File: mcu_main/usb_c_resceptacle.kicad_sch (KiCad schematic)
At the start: 8 parts, among them U2 USB_C_connector

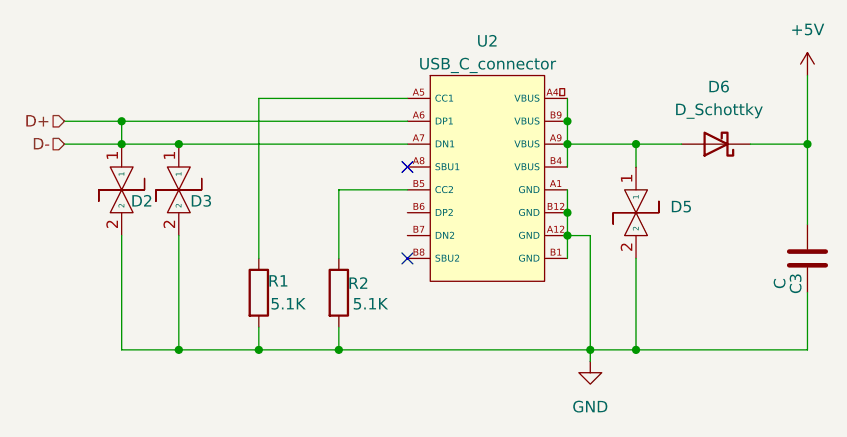
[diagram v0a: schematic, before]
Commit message: adding boot-reset buttons and microsd card spi
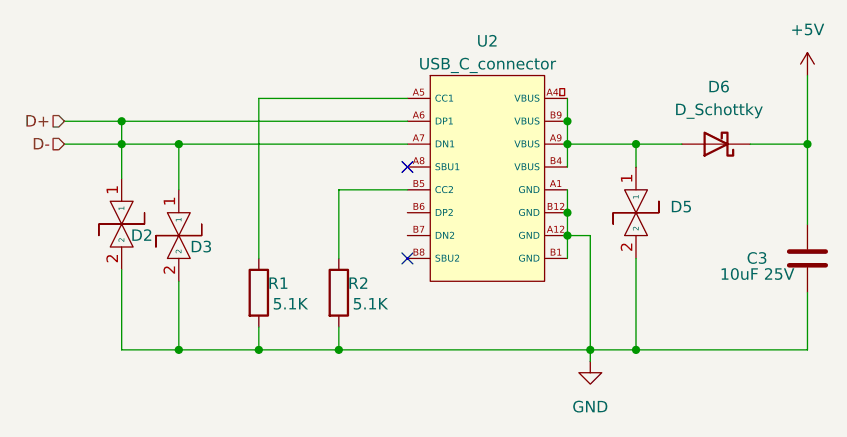
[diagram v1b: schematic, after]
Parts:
- C3: value C -> 10uF 25V
- D2, D3, D5: footprint (none) -> Diode_SMD:D_SOD-882
- R1, R2: footprint (none) -> Resistor_SMD:R_0805_2012Metric_Pad1.20x1.40mm_HandSolder
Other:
- moved on the sheet: D2, D3
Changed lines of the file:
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@@
+	(wire
+		(pts
+			(xy 121.92 96.52) (xy 121.92 91.44)
+		)
+		(stroke
+			(width 0)
+			(type default)
+		)
+	)
 	(wire
 		(pts
@@
 	(wire
 		(pts
+			(xy 115.57 95.25) (xy 115.57 91.44)
+		)
+		(stroke
+			(width 0)
+			(type default)
+		)
+	)
+	(wire
+		(pts
 			(xy 147.32 96.52) (xy 139.7 96.52)
 		)
@@
 	(wire
 		(pts
-			(xy 115.57 101.6) (xy 115.57 114.3)
+			(xy 115.57 105.41) (xy 115.57 114.3)
 		)
 		(stroke
@@
 	(wire
 		(pts
-			(xy 121.92 101.6) (xy 121.92 114.3)
+			(xy 121.92 106.68) (xy 121.92 114.3)
 		)
 		(stroke
@@
 	(symbol
 		(lib_id "Custom_symbols:ESD_protection_TVS_RCLAMP0521P-N")
-		(at 115.57 96.52 270)
+		(at 115.57 100.33 270)
 		(unit 1)
 		(exclude_from_sim no)
@@
 		(dnp no)
 		(property "Reference" "D2"
-			(at 116.586 97.79 90)
+			(at 116.586 101.6 90)
 			(effects
 				(font
@@
 		)
 		(property "Value" "~"
-			(at 119.38 97.79 90)
+			(at 119.38 101.6 90)
 			(effects
 				(font
@@
 			)
 		)
-		(property "Footprint" ""
-			(at 115.57 96.52 0)
-			(effects
-				(font
-					(size 1.27 1.27)
-				)
-				(hide yes)
-			)
-		)
-		(property "Datasheet" ""
-			(at 115.57 96.52 0)
+		(property "Footprint" "Diode_SMD:D_SOD-882"
+			(at 115.57 100.33 0)
+			(effects
+				(font
+					(size 1.27 1.27)
+				)
+				(hide yes)
+			)
+		)
+		(property "Datasheet" "https://www.lcsc.com/datasheet/lcsc_datasheet_2304171630_BORN-RCLAMP0521P-N_C316043.pdf"
+			(at 115.57 100.33 0)
 			(effects
 				(font
@@
 		)
 		(property "Description" ""
-			(at 115.57 96.52 0)
+			(at 115.57 100.33 0)
 			(effects
 				(font
@@
 			)
 		)
-		(property "Footprint" ""
+		(property "Footprint" "Diode_SMD:D_SOD-882"
 			(at 172.72 99.06 0)
 			(effects
@@
 			)
 		)
-		(property "Datasheet" ""
+		(property "Datasheet" "https://www.lcsc.com/datasheet/lcsc_datasheet_2304171630_BORN-RCLAMP0521P-N_C316043.pdf"
 			(at 172.72 99.06 0)
 			(effects
@@
 			)
 		)
-		(property "Datasheet" "~"
+		(property "Datasheet" "https://www.lcsc.com/datasheet/lcsc_datasheet_2411211953_MDD-Microdiode-Semiconductor-B5819W_C64885.pdf"
 			(at 181.61 91.44 0)
 			(effects
@@
 				(path "/8c1e5247-e001-4f3c-b236-a22b9c821843/832b2f07-429b-4c98-b10e-bc5206aa930b"
 					(reference "D6")
+					(unit 1)
+				)
+			)
+		)
+	)
+	(symbol
+		(lib_id "Device:R")
+		(at 130.81 107.95 0)
+		(unit 1)
+		(exclude_from_sim no)
+		(in_bom yes)
+		(on_board yes)
+		(dnp no)
+		(property "Reference" "R1"
+			(at 131.826 106.934 0)
+			(effects
+				(font
+					(size 1.27 1.27)
+				)
+				(justify left)
+			)
+		)
+		(property "Value" "5.1K"
+			(at 132.334 109.22 0)
+			(effects
+				(font
+					(size 1.27 1.27)
+				)
+				(justify left)
+			)
+		)
+		(property "Footprint" "Resistor_SMD:R_0805_2012Metric_Pad1.20x1.40mm_HandSolder"
+			(at 129.032 107.95 90)
+			(effects
+				(font
+					(size 1.27 1.27)
+				)
+				(hide yes)
+			)
+		)
+		(property "Datasheet" "~"
+			(at 130.81 107.95 0)
+			(effects
+				(font
+					(size 1.27 1.27)
+				)
+				(hide yes)
+			)
+		)
+		(property "Description" "Resistor"
+			(at 130.81 107.95 0)
+			(effects
+				(font
+					(size 1.27 1.27)
+				)
+				(hide yes)
+			)
+		)
+		(pin "2"
+		)
+		(pin "1"
+		)
+		(instances
+			(project "mcu_main"
+				(path "/8c1e5247-e001-4f3c-b236-a22b9c821843/832b2f07-429b-4c98-b10e-bc5206aa930b"
+					(reference "R1")
 					(unit 1)
 				)
@@
 			)
 		)
-		(property "Footprint" ""
+		(property "Footprint" "Resistor_SMD:R_0805_2012Metric_Pad1.20x1.40mm_HandSolder"
 			(at 137.922 107.95 90)
 			(effects
@@
 	)
 	(symbol
-		(lib_id "Device:R")
-		(at 130.81 107.95 0)
-		(unit 1)
-		(exclude_from_sim no)
-		(in_bom yes)
-		(on_board yes)
-		(dnp no)
-		(property "Reference" "R1"
-			(at 131.826 106.68 0)
-			(effects
-				(font
-					(size 1.27 1.27)
-				)
-				(justify left)
-			)
-		)
-		(property "Value" "5.1K"
-			(at 132.08 109.22 0)
-			(effects
-				(font
-					(size 1.27 1.27)
-				)
-				(justify left)
-			)
-		)
-		(property "Footprint" ""
-			(at 129.032 107.95 90)
-			(effects
-				(font
-					(size 1.27 1.27)
-				)
-				(hide yes)
-			)
-		)
-		(property "Datasheet" "~"
-			(at 130.81 107.95 0)
-			(effects
-				(font
-					(size 1.27 1.27)
-				)
-				(hide yes)
-			)
-		)
-		(property "Description" "Resistor"
-			(at 130.81 107.95 0)
-			(effects
-				(font
-					(size 1.27 1.27)
-				)
-				(hide yes)
-			)
-		)
-		(pin "2"
-		)
-		(pin "1"
-		)
-		(instances
-			(project "mcu_main"
-				(path "/8c1e5247-e001-4f3c-b236-a22b9c821843/832b2f07-429b-4c98-b10e-bc5206aa930b"
-					(reference "R1")
-					(unit 1)
-				)
-			)
-		)
-	)
-	(symbol
 		(lib_id "Custom_symbols:ESD_protection_TVS_RCLAMP0521P-N")
-		(at 121.92 96.52 270)
+		(at 121.92 101.6 270)
 		(unit 1)
 		(exclude_from_sim no)
@@
 		(dnp no)
 		(property "Reference" "D3"
-			(at 123.19 97.79 90)
+			(at 123.19 102.87 90)
 			(effects
 				(font
@@
 		)
 		(property "Value" "~"
-			(at 125.73 97.79 90)
+			(at 125.73 102.87 90)
 			(effects
 				(font
@@
 			)
 		)
-		(property "Footprint" ""
-			(at 121.92 96.52 0)
-			(effects
-				(font
-					(size 1.27 1.27)
-				)
-				(hide yes)
-			)
-		)
-		(property "Datasheet" ""
-			(at 121.92 96.52 0)
+		(property "Footprint" "Diode_SMD:D_SOD-882"
+			(at 121.92 101.6 0)
+			(effects
+				(font
+					(size 1.27 1.27)
+				)
+				(hide yes)
+			)
+		)
+		(property "Datasheet" "https://www.lcsc.com/datasheet/lcsc_datasheet_2304171630_BORN-RCLAMP0521P-N_C316043.pdf"
+			(at 121.92 101.6 0)
 			(effects
 				(font
@@
 		)
 		(property "Description" ""
-			(at 121.92 96.52 0)
+			(at 121.92 101.6 0)
 			(effects
 				(font
@@
 		(dnp no)
 		(property "Reference" "C3"
-			(at 190.5 106.934 90)
-			(effects
-				(font
-					(size 1.27 1.27)
-				)
-			)
-		)
-		(property "Value" "C"
-			(at 188.722 106.934 90)
-			(effects
-				(font
+			(at 186.182 104.14 0)
+			(effects
+				(font
+					(size 1.27 1.27)
+				)
+			)
+		)
+		(property "Value" "10uF 25V"
+			(at 186.182 105.918 0)
+			(effects
+				(font

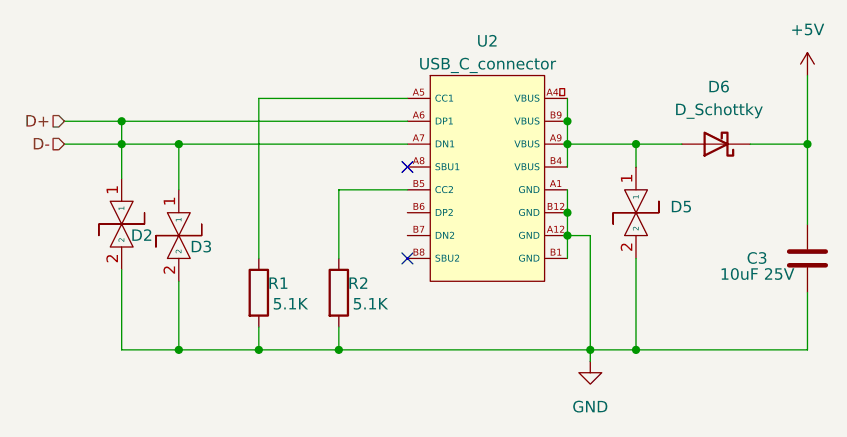
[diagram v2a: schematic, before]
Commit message: Added connections for the display SPI
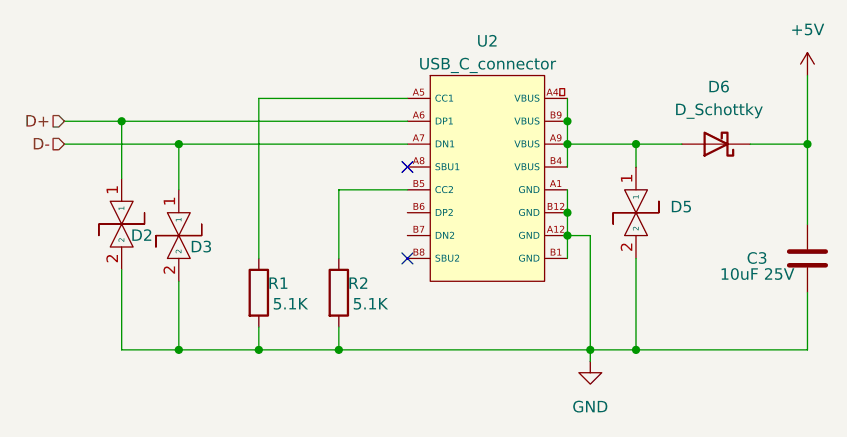
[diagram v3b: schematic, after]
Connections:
- net D+: no longer D3.1, U2.A7 (DN1)
- new net D-: D3.1, U2.A7 (DN1)
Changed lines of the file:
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@@
-	)
-	(junction
-		(at 115.57 91.44)
-		(diameter 0)
-		(color 0 0 0 0)
 	)
 	(junction
@@
 	(wire
 		(pts
-			(xy 115.57 91.44) (xy 121.92 91.44)
+			(xy 109.22 91.44) (xy 121.92 91.44)
 		)
 		(stroke
@@
 	(wire
 		(pts
-			(xy 109.22 91.44) (xy 115.57 91.44)
-		)
-		(stroke
-			(width 0)
-			(type default)
-		)
-	)
-	(wire
-		(pts
 			(xy 115.57 114.3) (xy 121.92 114.3)
 		)
@@
 	(wire
 		(pts
-			(xy 115.57 95.25) (xy 115.57 91.44)
+			(xy 115.57 88.9) (xy 115.57 95.25)
 		)
 		(stroke
@@
 		)
 		(stroke
-			(width 0)
-			(type default)
-		)
-	)
-	(wire
-		(pts
-			(xy 115.57 91.44) (xy 115.57 88.9)
-		)
-		(stroke

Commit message: ERC done and fixed
most of the stuff was fine, except needed to fix the power pins on the tvs diode symbol
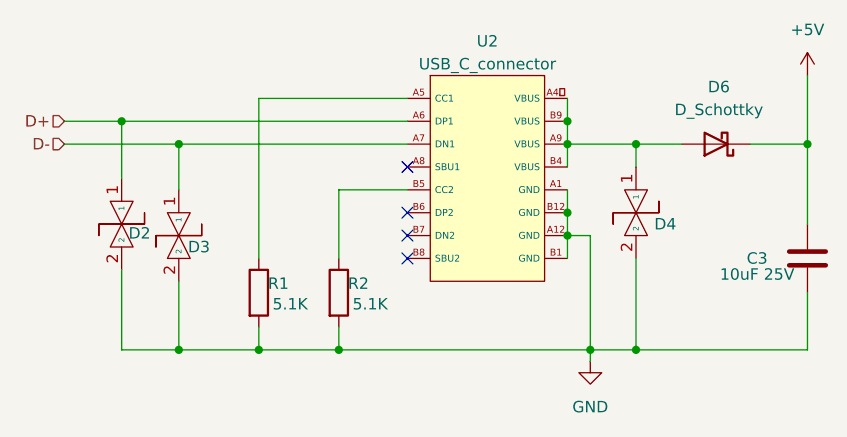
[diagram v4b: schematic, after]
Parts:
- removed D5: ~, Diode_SMD:D_SOD-882, symbol Custom_symbols:ESD_protection_TVS_RCLAMP0521P-N
- added D4: ~, Diode_SMD:D_SOD-882, symbol Custom_symbols:ESD_protection_TVS_RCLAMP0521P-N
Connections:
- net GND: now also D4.2
- net at D6.2 (A), U2.A4  (VBUS), U2.A9 (VBUS)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: now also D4.1
- no-connect marks 2 -> 4
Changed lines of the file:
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@@
+	)
+	(no_connect
+		(at 147.32 101.6)
 	)
 	(no_connect
 		(at 147.32 93.98)
+	)
+	(no_connect
+		(at 147.32 99.06)
 	)
 	(wire
@@
 	(symbol
 		(lib_id "Custom_symbols:ESD_protection_TVS_RCLAMP0521P-N")
-		(at 115.57 100.33 270)
+		(at 121.92 101.6 270)
 		(unit 1)
 		(exclude_from_sim no)
@@
 		(on_board yes)
 		(dnp no)
-		(property "Reference" "D2"
-			(at 116.586 101.6 90)
+		(property "Reference" "D3"
+			(at 122.936 102.87 90)
 			(effects
 				(font
@@
 		)
 		(property "Value" "~"
-			(at 119.38 101.6 90)
+			(at 125.73 102.87 90)
 			(effects
 				(font
@@
 		)
 		(property "Footprint" "Diode_SMD:D_SOD-882"
-			(at 115.57 100.33 0)
+			(at 121.92 101.6 0)
 			(effects
 				(font
@@
 		)
 		(property "Datasheet" "https://www.lcsc.com/datasheet/lcsc_datasheet_2304171630_BORN-RCLAMP0521P-N_C316043.pdf"
-			(at 115.57 100.33 0)
+			(at 121.92 101.6 0)
 			(effects
 				(font
@@
 		)
 		(property "Description" ""
-			(at 115.57 100.33 0)
+			(at 121.92 101.6 0)
 			(effects
 				(font
@@
 			(project "mcu_main"
 				(path "/8c1e5247-e001-4f3c-b236-a22b9c821843/832b2f07-429b-4c98-b10e-bc5206aa930b"
-					(reference "D2")
+					(reference "D3")
 					(unit 1)
 				)
@@
 	)
 	(symbol
-		(lib_id "Custom_symbols:ESD_protection_TVS_RCLAMP0521P-N")
-		(at 172.72 99.06 270)
-		(unit 1)
-		(exclude_from_sim no)
-		(in_bom yes)
-		(on_board yes)
-		(dnp no)
-		(fields_autoplaced yes)
-		(property "Reference" "D5"
-			(at 176.53 98.4249 90)
-			(effects
-				(font
-					(size 1.27 1.27)
-				)
-				(justify left)
-			)
-		)
-		(property "Value" "~"
-			(at 176.53 100.33 90)
-			(effects
-				(font
-					(size 1.27 1.27)
-				)
-				(justify left)
-			)
-		)
-		(property "Footprint" "Diode_SMD:D_SOD-882"
-			(at 172.72 99.06 0)
-			(effects
-				(font
-					(size 1.27 1.27)
-				)
-				(hide yes)
-			)
-		)
-		(property "Datasheet" "https://www.lcsc.com/datasheet/lcsc_datasheet_2304171630_BORN-RCLAMP0521P-N_C316043.pdf"
-			(at 172.72 99.06 0)
-			(effects
-				(font
-					(size 1.27 1.27)
-				)
-				(hide yes)
-			)
-		)
-		(property "Description" ""
-			(at 172.72 99.06 0)
-			(effects
-				(font
-					(size 1.27 1.27)
-				)
-				(hide yes)
-			)
-		)
-		(pin "2"
-		)
-		(pin "1"
-		)
-		(instances
-			(project "mcu_main"
-				(path "/8c1e5247-e001-4f3c-b236-a22b9c821843/832b2f07-429b-4c98-b10e-bc5206aa930b"
-					(reference "D5")
-					(unit 1)
-				)
-			)
-		)
-	)
-	(symbol
 		(lib_id "power:GND")
 		(at 167.64 115.57 0)
@@
 	)
 	(symbol
+		(lib_id "Custom_symbols:ESD_protection_TVS_RCLAMP0521P-N")
+		(at 172.72 99.06 270)
+		(unit 1)
+		(exclude_from_sim no)
+		(in_bom yes)
+		(on_board yes)
+		(dnp no)
+		(property "Reference" "D4"
+			(at 174.752 100.33 90)
+			(effects
+				(font
+					(size 1.27 1.27)
+				)
+				(justify left)
+			)
+		)
+		(property "Value" "~"
+			(at 176.53 100.33 90)
+			(effects
+				(font
+					(size 1.27 1.27)
+				)
+				(justify left)
+			)
+		)
+		(property "Footprint" "Diode_SMD:D_SOD-882"
+			(at 172.72 99.06 0)
+			(effects
+				(font
+					(size 1.27 1.27)
+				)
+				(hide yes)
+			)
+		)
+		(property "Datasheet" "https://www.lcsc.com/datasheet/lcsc_datasheet_2304171630_BORN-RCLAMP0521P-N_C316043.pdf"
+			(at 172.72 99.06 0)
+			(effects
+				(font
+					(size 1.27 1.27)
+				)
+				(hide yes)
+			)
+		)
+		(property "Description" ""
+			(at 172.72 99.06 0)
+			(effects
+				(font
+					(size 1.27 1.27)
+				)
+				(hide yes)
+			)
+		)
+		(pin "2"
+		)
+		(pin "1"
+		)
+		(instances
+			(project "mcu_main"
+				(path "/8c1e5247-e001-4f3c-b236-a22b9c821843/832b2f07-429b-4c98-b10e-bc5206aa930b"
+					(reference "D4")
+					(unit 1)
+				)
+			)
+		)
+	)
+	(symbol
 		(lib_id "Device:R")
 		(at 139.7 107.95 0)
@@
 	(symbol
 		(lib_id "Custom_symbols:ESD_protection_TVS_RCLAMP0521P-N")
-		(at 121.92 101.6 270)
+		(at 115.57 100.33 270)
 		(unit 1)
 		(exclude_from_sim no)
@@
 		(on_board yes)
 		(dnp no)
-		(property "Reference" "D3"
-			(at 123.19 102.87 90)
+		(property "Reference" "D2"
+			(at 116.332 101.346 90)
 			(effects
 				(font
@@
 		)
 		(property "Value" "~"
-			(at 125.73 102.87 90)
+			(at 119.38 101.6 90)
 			(effects
 				(font
@@
 		)
 		(property "Footprint" "Diode_SMD:D_SOD-882"
-			(at 121.92 101.6 0)
+			(at 115.57 100.33 0)
 			(effects
 				(font
@@
 		)
 		(property "Datasheet" "https://www.lcsc.com/datasheet/lcsc_datasheet_2304171630_BORN-RCLAMP0521P-N_C316043.pdf"
-			(at 121.92 101.6 0)
+			(at 115.57 100.33 0)
 			(effects
 				(font
@@
 		)
 		(property "Description" ""
-			(at 121.92 101.6 0)
+			(at 115.57 100.33 0)
 			(effects
 				(font
@@
 		)
 		(instances
-			(project "mcu_main"
+			(project ""
 				(path "/8c1e5247-e001-4f3c-b236-a22b9c821843/832b2f07-429b-4c98-b10e-bc5206aa930b"
-					(reference "D3")
+					(reference "D2")
 					(unit 1)
 				)

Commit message: started pcb layout
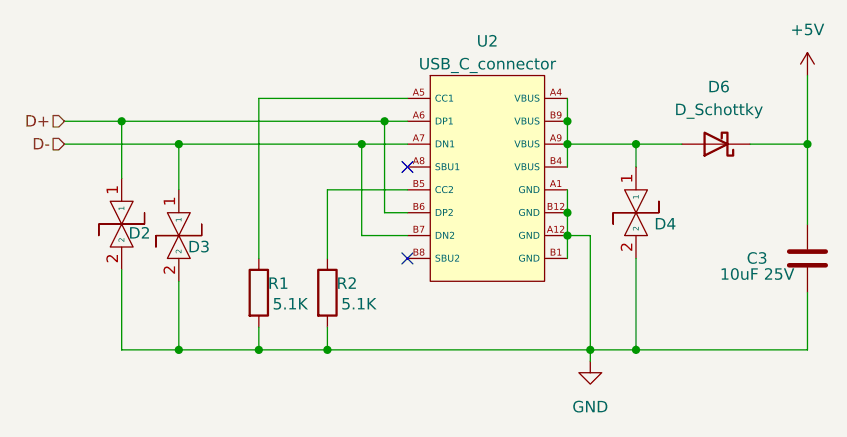
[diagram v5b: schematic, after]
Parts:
- U2: footprint Connector_USB:USB_C_Receptacle_G-Switch_GT-USB-7010ASV -> Connector_USB:USB_C_Receptacle_Amphenol_12401948E412A
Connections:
- net D+: now also U2.B6 (DP2)
- net D-: now also U2.B7 (DN2)
- net at D4.1, D6.2 (A), U2.A9 (VBUS)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: now also U2.A4 (VBUS); no longer U2.A4  (VBUS)
- no-connect marks 4 -> 2
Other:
- moved on the sheet: R2

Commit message: Fixed most drc violations
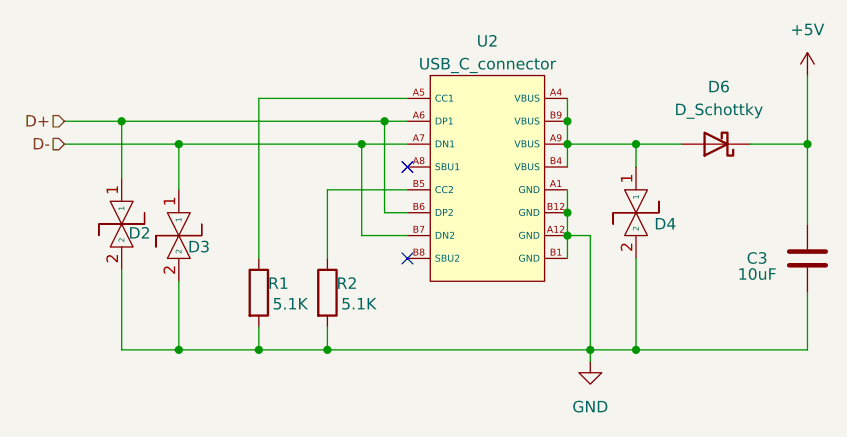
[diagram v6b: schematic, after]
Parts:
- C3: value 10uF 25V -> 10uF
- U2: footprint Connector_USB:USB_C_Receptacle_Amphenol_12401948E412A -> Custom_footprints:USB_C_Receptacle_Amphenol_12401948E412A_editted
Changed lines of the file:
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@@
 			)
 		)
-		(property "Footprint" "Connector_USB:USB_C_Receptacle_Amphenol_12401948E412A"
+		(property "Footprint" "Custom_footprints:USB_C_Receptacle_Amphenol_12401948E412A_editted"
 			(at 156.21 95.25 0)
 			(effects
@@
 			)
 		)
-		(property "Value" "10uF 25V"
+		(property "Value" "10uF"
 			(at 186.182 105.918 0)
 			(effects
